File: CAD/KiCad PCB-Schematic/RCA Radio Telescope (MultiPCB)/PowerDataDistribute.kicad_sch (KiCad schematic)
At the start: 32 parts, among them J7 USB_A, J8 USB_A, Q1 DMP4047LFDE-7, U13 MAX8510EXK30T, U14 TPS62133RGTR

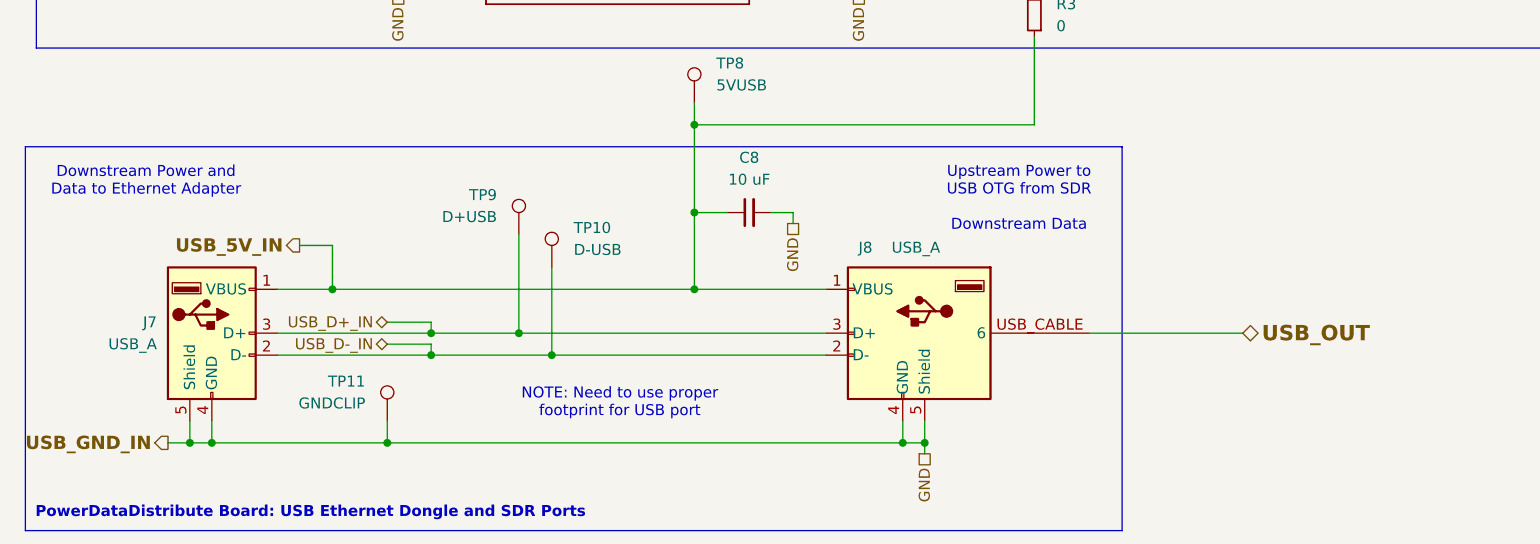
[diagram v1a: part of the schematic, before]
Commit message: Updated Schematic to Fix USB/PMOS issues and Minor Fixes
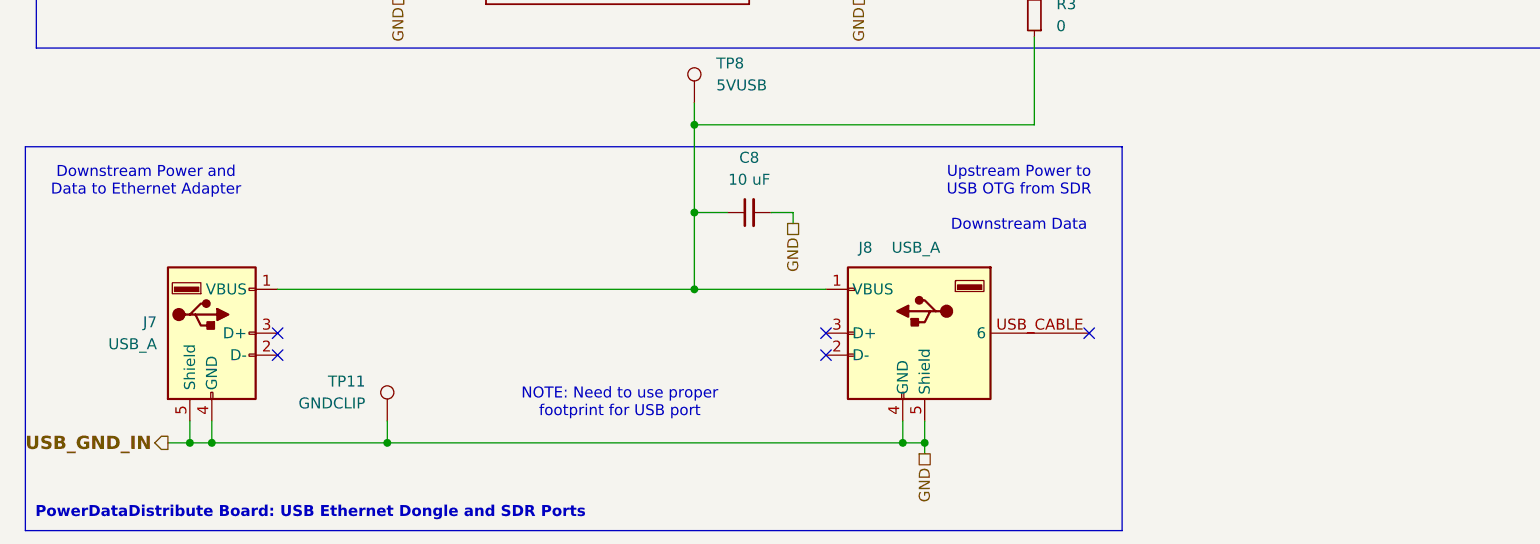
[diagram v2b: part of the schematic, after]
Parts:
- removed TP10: D-USB, Library:TestPoint_Pad_D1.0mm_Edit, symbol Connector:TestPoint
- removed TP9: D+USB, Library:TestPoint_Pad_D1.0mm_Edit, symbol Connector:TestPoint
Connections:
- net USB_5V_IN: no longer names the net of C8.1, J7.1 (VBUS), J8.1 (VBUS), R3.1, TP8.1
- net USB_D+_IN: no longer names the net of J8.3 (D+)
- net USB_D+_IN: no longer J7.3 (D+)
- net USB_D-_IN: no longer names the net of J8.2 (D-)
- net USB_D-_IN: no longer J7.2 (D-)
- net USB_OUT: no longer names the net of J8.USB_CABLE (6)
- no-connect marks 0 -> 5
